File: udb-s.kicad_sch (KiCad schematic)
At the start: 9 parts, among them J1 TYPE-C-31-M-12, J2 SM04B-SRSS, U2 USBLC6-2SC6

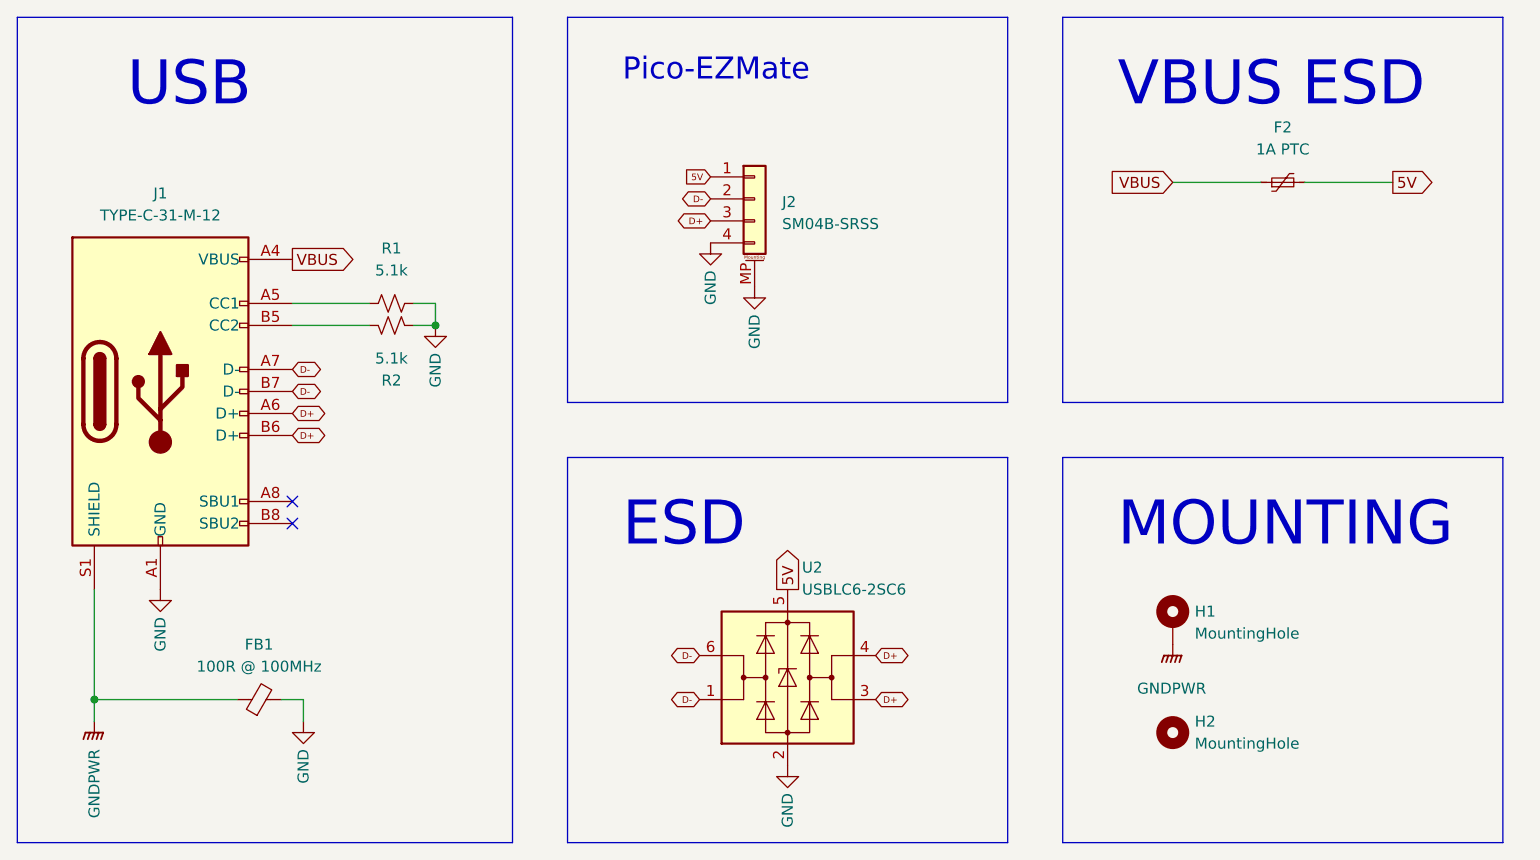
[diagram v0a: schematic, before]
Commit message: Adjusted ferrite bead location and changed mousebites
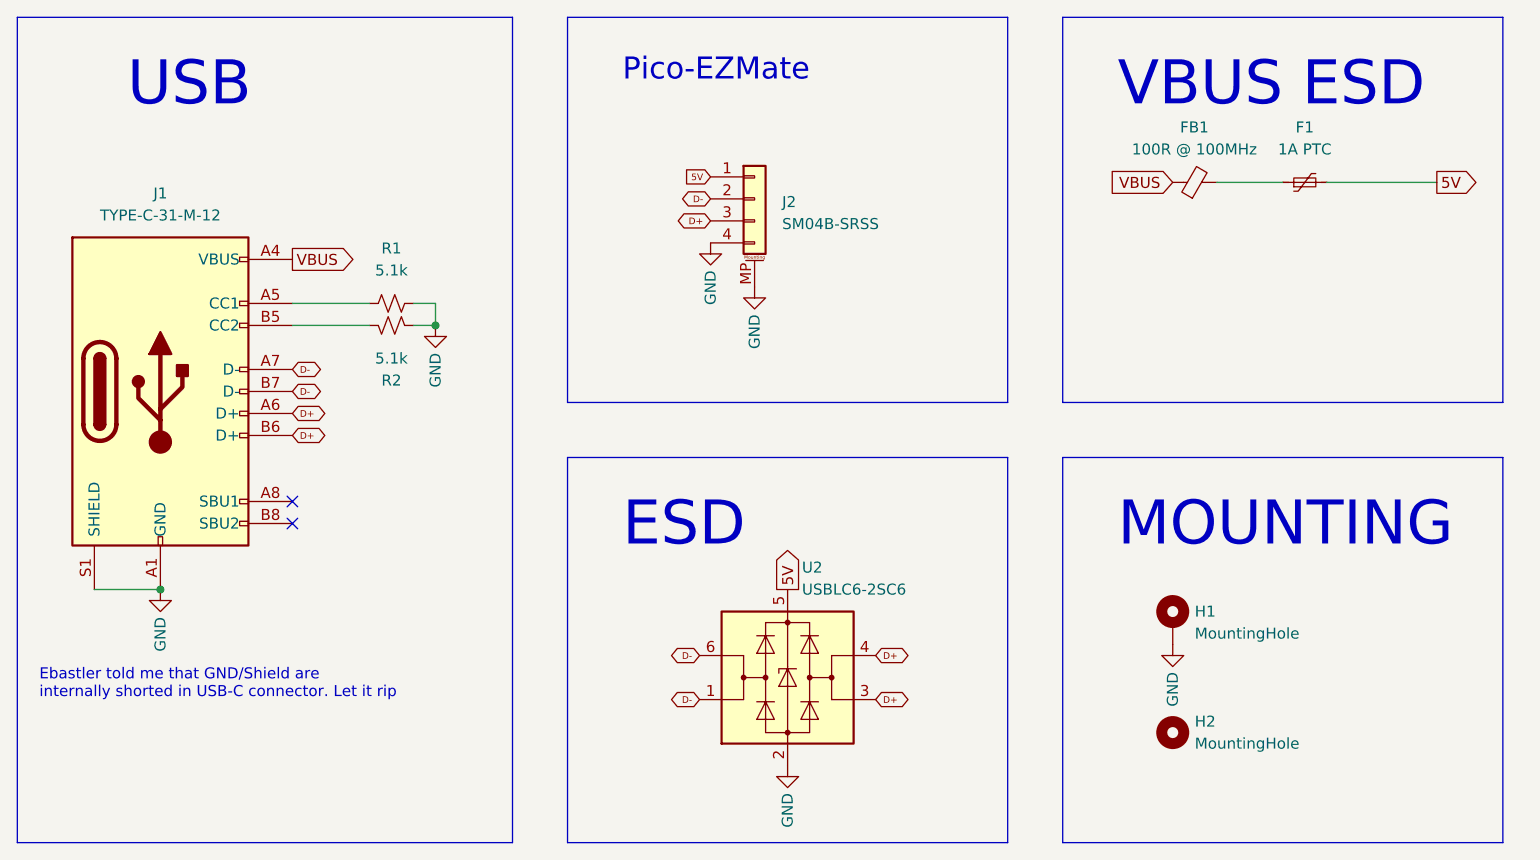
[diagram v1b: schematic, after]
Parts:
- removed F2: 1A PTC, Fuse:Fuse_0402_1005Metric, symbol Device:Polyfuse_Small
- added F1: 1A PTC, Fuse:Fuse_0402_1005Metric, symbol Device:Polyfuse_Small
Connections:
- net 5V: now also F1.2
- net GND: now also H1.1, J1.S1 (SHIELD); no longer FB1.2
- net VBUS: now also FB1.1
- removed net GNDPWR: FB1.1, H1.1, J1.S1 (SHIELD)
- new net: F1.1, FB1.2
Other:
- note added: "Ebastler told me that GND/Shield are internally shorted in USB-C connector. Let it rip"
